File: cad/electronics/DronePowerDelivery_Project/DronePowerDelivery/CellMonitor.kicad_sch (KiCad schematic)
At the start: 12 parts, among them J1 Conn_01x05_Socket, J2 Conn_01x02_Socket, U1 BQ76920PW

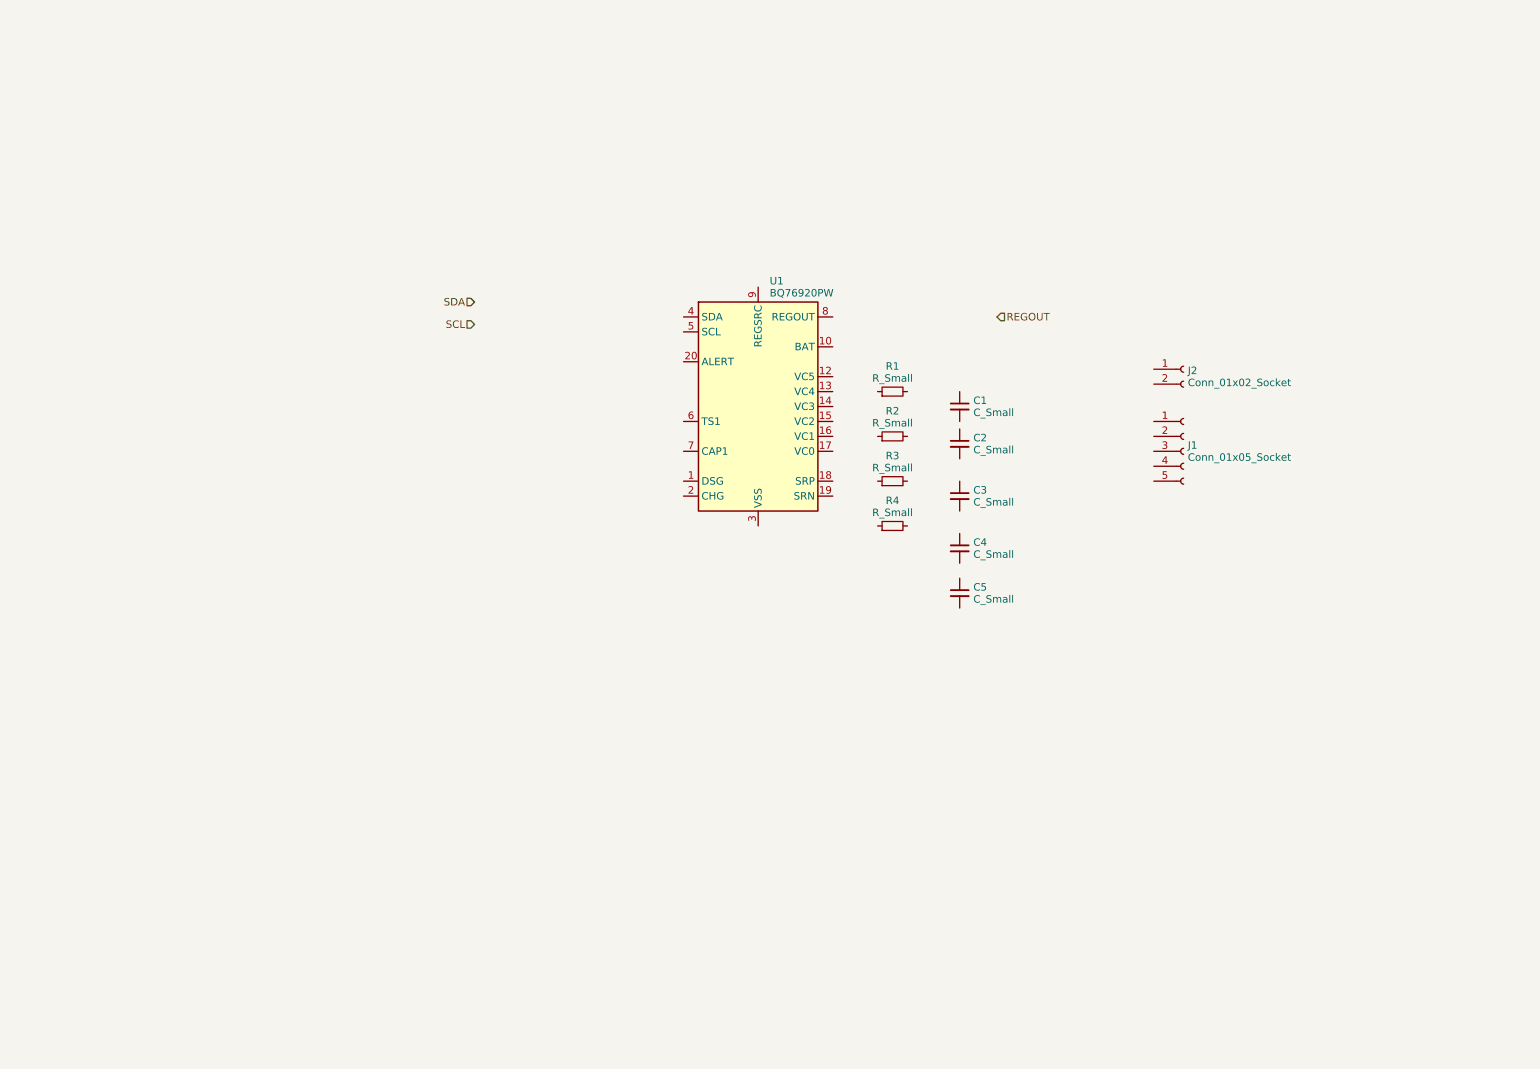
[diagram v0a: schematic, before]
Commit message: Added additional schematic capture
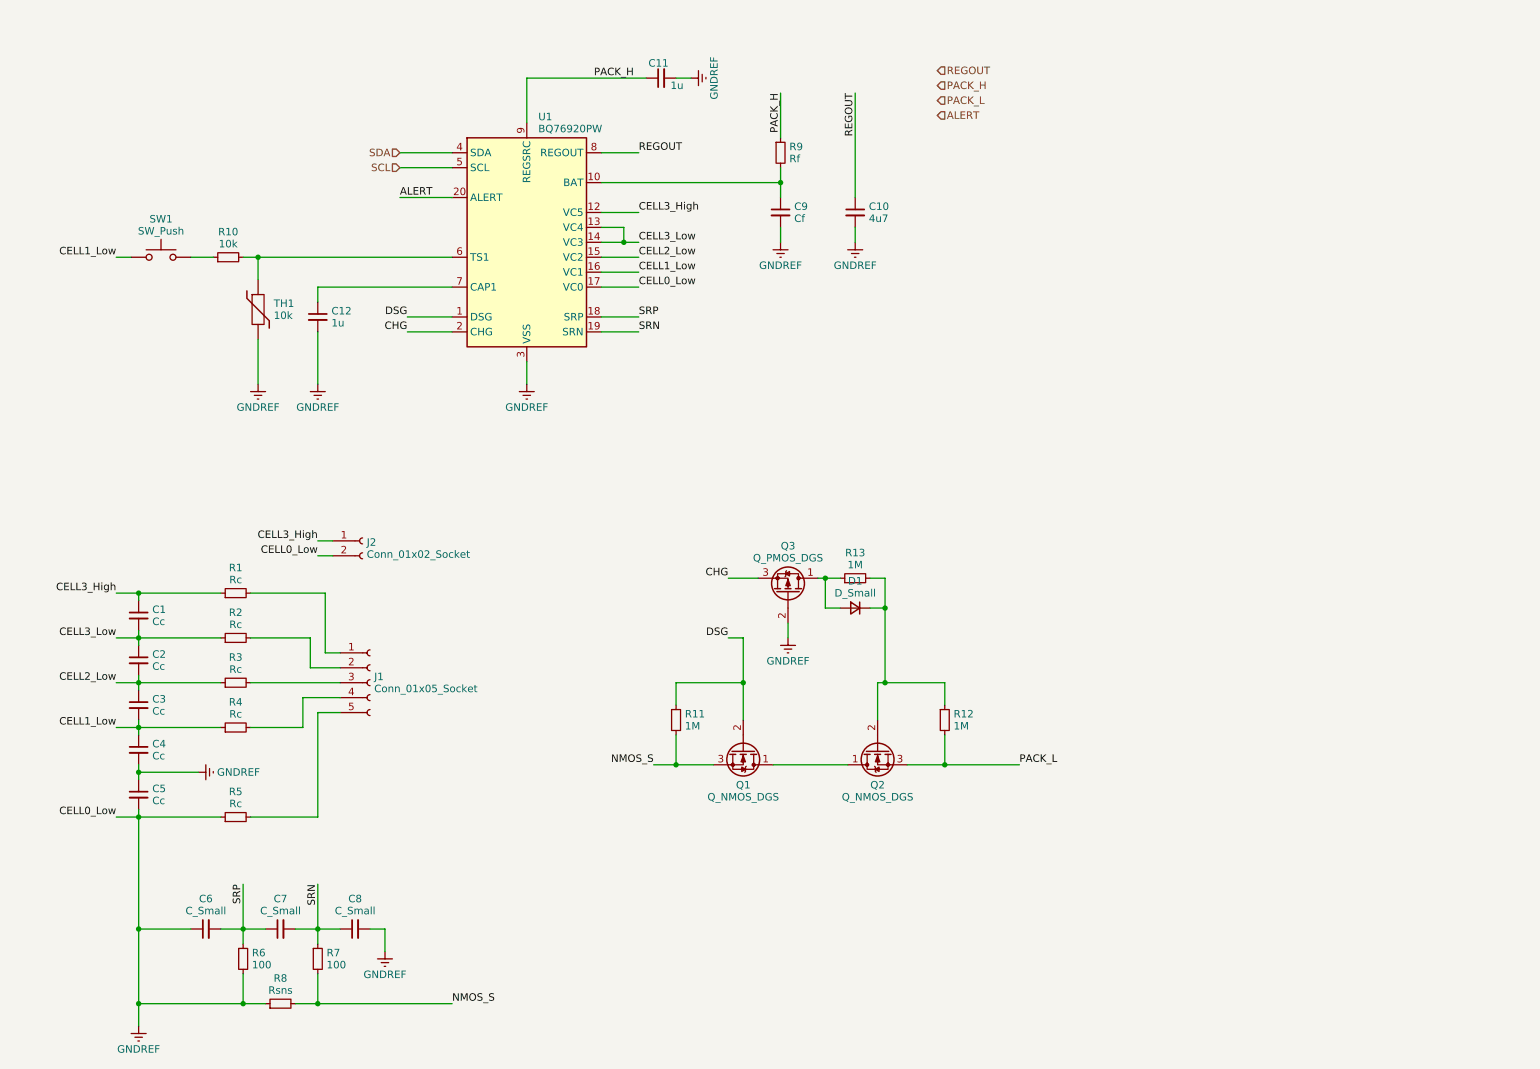
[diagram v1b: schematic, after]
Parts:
- added C10: 4u7, symbol Device:C_Small
- added C11, C12: 1u, symbol Device:C_Small
- added C6, C7, C8: C_Small, symbol Device:C_Small
- added C9: Cf, symbol Device:C_Small
- added D1: D_Small, symbol Device:D_Small
- added Q1, Q2: Q_NMOS_DGS, symbol Device:Q_NMOS_DGS
- added Q3: Q_PMOS_DGS, symbol Device:Q_PMOS_DGS
- added R10: 10k, symbol Device:R_Small
- added R11, R12, R13: 1M, symbol Device:R_Small
- added R5: Rc, symbol Device:R_Small
- added R6, R7: 100, symbol Device:R_Small
- added R8: Rsns, symbol Device:R_Small
- added R9: Rf, symbol Device:R_Small
- added SW1: SW_Push, symbol Switch:SW_Push
- added TH1: 10k, symbol Device:Thermistor
- C1, C2, C3, C4, C5: value C_Small -> Cc
- R1, R2, R3, R4: value R_Small -> Rc
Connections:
- net REGOUT: now also U1.8 (REGOUT), C10.1
- net SCL: now also U1.5 (SCL)
- net SDA: now also U1.4 (SDA)
- net CELL3_High: now reaches C1.1
- net CELL3_High: now also J2.1 (Pin_1), R1.1, U1.12 (VC5)
- net CELL3_Low: now reaches C1.2
- net CELL3_Low: now also C2.1, R2.1, U1.13 (VC4), U1.14 (VC3)
- net at J1.1 (Pin_1): now also R1.2
- net at J1.2 (Pin_2): now also R2.2
- net at J1.3 (Pin_3): now also R3.2
- net at J1.4 (Pin_4): now also R4.2
- net at J1.5 (Pin_5): now also R5.2
- net CELL2_Low: now reaches C3.1
- net CELL2_Low: now also C2.2, R3.1, U1.15 (VC2)
- net CELL1_Low: now reaches C3.2
- net CELL1_Low: now also C4.1, R4.1, U1.16 (VC1), SW1.1
- net GNDREF: now reaches C4.2
- net GNDREF: now also C5.1, C5.2, J2.2 (Pin_2), U1.17 (VC0), U1.3 (VSS), C10.2, C11.2, C12.2, C6.1, C8.2, C9.2, Q3.2 (G), R5.1, R6.2, R8.1, TH1.2
- net DSG: now reaches U1.1 (DSG)
- net DSG: now also Q1.2 (G), R11.1
- net at U1.10 (BAT): now also C9.1, R9.2
- net SRP: now reaches U1.18 (SRP)
- net SRP: now also C6.2, C7.1, R6.1
- net SRN: now reaches U1.19 (SRN)
- net SRN: now also C7.2, C8.1, R7.1
- net CHG: now reaches U1.2 (CHG)
- net CHG: now also Q3.3 (S)
- net ALERT: now reaches U1.20 (ALERT)
- net at U1.6 (TS1): now also R10.2, TH1.1
- net at U1.7 (CAP1): now also C12.1
- net PACK_H: now reaches U1.9 (REGSRC)
- net PACK_H: now also C11.1, R9.1
- new net: R10.1, SW1.2
- new net: Q1.1 (D), Q2.1 (D)
- new net: D1.1 (K), Q2.2 (G), R12.1, R13.2
- new net: D1.2 (A), Q3.1 (D), R13.1
- new net NMOS_S: Q1.3 (S), R11.2, R7.2, R8.2
- new net PACK_L: Q2.3 (S), R12.2
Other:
- moved on the sheet: C1, C2, C3, C4, C5, J1, J2, R1, R2, R3, R4, U1

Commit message: Finialized Component Sizing
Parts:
- removed Q1, Q2: Q_NMOS_DGS, symbol Device:Q_NMOS_DGS
- removed Q3: Q_PMOS_DGS, symbol Device:Q_PMOS_DGS
- added Q1, Q2: Q_NMOS_GDS, Package_TO_SOT_SMD:TO-252-2, symbol Device:Q_NMOS_GDS
- added Q3: Q_PMOS_GSD, Package_TO_SOT_SMD:SOT-23, symbol Device:Q_PMOS_GSD
- C1, C10, C11, C12, C2, C3, C4, C5, C6, C7, C8, C9: footprint (none) -> Capacitor_SMD:C_0603_1608Metric
- D1: footprint (none) -> Diode_SMD:D_0603_1608Metric
- J1: footprint (none) -> Connector_JST:JST_XH_B5B-XH-A_1x05_P2.50mm_Vertical
- J2: footprint (none) -> Connector_AMASS:AMASS_XT60-F_1x02_P7.20mm_Vertical
- R1, R10, R11, R12, R13, R2, R3, R4, R5, R6, R7, R9, TH1: footprint (none) -> Resistor_SMD:R_0603_1608Metric
- R8: footprint (none) -> Resistor_SMD:R_2512_6332Metric
- SW1: footprint (none) -> Button_Switch_SMD:SW_SPST_EVQP2; Mfg Part# (none) -> EVQ-P2002W
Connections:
- net CELL3_High: no longer J2.1 (Pin_1)
- net CHG: now also Q3.2 (S)
- net DSG: now also Q1.1 (G)
- net GNDREF: now also J1.5 (Pin_5), J2.1 (Pin_1), R5.2, Q3.1 (G); no longer C5.2, J2.2 (Pin_2), R5.1, U1.17 (VC0)
- net PACK_H: now also J1.1 (Pin_1), J2.2 (Pin_2), R1.2
- net PACK_L: now also Q2.3 (S)
- net IN_PROT: now reaches D1.1 (K), R12.1, R13.2
- net IN_PROT: now also Q2.1 (G)
- net at D1.2 (A), R13.1: now also Q3.3 (D)
- net NMOS_S renamed Q1_SRC
- net Q1_SRC: now also Q1.3 (S)
- new net CELL0_Low: C5.2, R5.1, U1.17 (VC0)
- new net Q_DRN: Q1.2 (D), Q2.2 (D)
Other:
- note added: "Cell Voltage Probes & Balacing"
- note added: "Charge/Discharge Control Circuit"
- note added: "Current Sense Circuit"
- moved on the sheet: D1, J2, R11, R12, R13

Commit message: Assigned component values
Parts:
- C1, C2, C3, C4, C5: value Cc -> 1uf
- C6, C7, C8: value C_Small -> 0.1uf
- C9: value Cf -> 10uf
- R1, R2, R3, R4, R5: value Rc -> 100
- R9: value Rf -> 100
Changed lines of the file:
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@@
   (symbol (lib_id "Device:R_Small") (at 154.94 38.1 0) (unit 1)
     (in_bom yes) (on_board yes) (dnp no) (fields_autoplaced)
-    (property "Reference" "R9" (at 156.4386 37.076 0)
-      (effects (font (size 1.27 1.27)) (justify left))
-    )
-    (property "Value" "Rf" (at 156.4386 39.124 0)
+    (property "Reference" "R9" (at 156.4386 36.8879 0)
+      (effects (font (size 1.27 1.27)) (justify left))
+    )
+    (property "Value" "100" (at 156.4386 39.3121 0)
       (effects (font (size 1.27 1.27)) (justify left))
     )
@@
   (symbol (lib_id "Device:C_Small") (at 45.72 116.84 0) (unit 1)
     (in_bom yes) (on_board yes) (dnp no) (fields_autoplaced)
-    (property "Reference" "C1" (at 48.0441 115.8223 0)
-      (effects (font (size 1.27 1.27)) (justify left))
-    )
-    (property "Value" "Cc" (at 48.0441 117.8703 0)
+    (property "Reference" "C1" (at 48.0441 115.6342 0)
+      (effects (font (size 1.27 1.27)) (justify left))
+    )
+    (property "Value" "1uf" (at 48.0441 118.0584 0)
       (effects (font (size 1.27 1.27)) (justify left))
     )
@@
   (symbol (lib_id "Device:C_Small") (at 57.15 170.18 90) (unit 1)
     (in_bom yes) (on_board yes) (dnp no) (fields_autoplaced)
-    (property "Reference" "C6" (at 57.1563 165.0379 90)
-      (effects (font (size 1.27 1.27)))
-    )
-    (property "Value" "C_Small" (at 57.1563 167.0859 90)
+    (property "Reference" "C6" (at 57.1563 164.4736 90)
+      (effects (font (size 1.27 1.27)))
+    )
+    (property "Value" "0.1uf" (at 57.1563 166.8978 90)
       (effects (font (size 1.27 1.27)))
     )
@@
   (symbol (lib_id "Device:R_Small") (at 62.23 151.13 90) (unit 1)
     (in_bom yes) (on_board yes) (dnp no) (fields_autoplaced)
-    (property "Reference" "R5" (at 62.23 146.8134 90)
-      (effects (font (size 1.27 1.27)))
-    )
-    (property "Value" "Rc" (at 62.23 148.8614 90)
+    (property "Reference" "R5" (at 62.23 146.2491 90)
+      (effects (font (size 1.27 1.27)))
+    )
+    (property "Value" "100" (at 62.23 148.6733 90)
       (effects (font (size 1.27 1.27)))
     )
@@
   (symbol (lib_id "Device:C_Small") (at 69.85 170.18 90) (unit 1)
     (in_bom yes) (on_board yes) (dnp no) (fields_autoplaced)
-    (property "Reference" "C7" (at 69.8563 165.0379 90)
-      (effects (font (size 1.27 1.27)))
-    )
-    (property "Value" "C_Small" (at 69.8563 167.0859 90)
+    (property "Reference" "C7" (at 69.8563 164.4736 90)
+      (effects (font (size 1.27 1.27)))
+    )
+    (property "Value" "0.1uf" (at 69.8563 166.8978 90)
       (effects (font (size 1.27 1.27)))
     )
@@
   (symbol (lib_id "Device:C_Small") (at 45.72 132.08 0) (unit 1)
     (in_bom yes) (on_board yes) (dnp no) (fields_autoplaced)
-    (property "Reference" "C3" (at 48.0441 131.0623 0)
-      (effects (font (size 1.27 1.27)) (justify left))
-    )
-    (property "Value" "Cc" (at 48.0441 133.1103 0)
+    (property "Reference" "C3" (at 48.0441 130.8742 0)
+      (effects (font (size 1.27 1.27)) (justify left))
+    )
+    (property "Value" "1uf" (at 48.0441 133.2984 0)
       (effects (font (size 1.27 1.27)) (justify left))
     )
@@
   (symbol (lib_id "Device:C_Small") (at 82.55 170.18 90) (unit 1)
     (in_bom yes) (on_board yes) (dnp no) (fields_autoplaced)
-    (property "Reference" "C8" (at 82.5563 165.0379 90)
-      (effects (font (size 1.27 1.27)))
-    )
-    (property "Value" "C_Small" (at 82.5563 167.0859 90)
+    (property "Reference" "C8" (at 82.5563 164.4736 90)
+      (effects (font (size 1.27 1.27)))
+    )
+    (property "Value" "0.1uf" (at 82.5563 166.8978 90)
       (effects (font (size 1.27 1.27)))
     )
@@
   (symbol (lib_id "Device:C_Small") (at 45.72 139.7 0) (unit 1)
     (in_bom yes) (on_board yes) (dnp no) (fields_autoplaced)
-    (property "Reference" "C4" (at 48.0441 138.6823 0)
-      (effects (font (size 1.27 1.27)) (justify left))
-    )
-    (property "Value" "Cc" (at 48.0441 140.7303 0)
+    (property "Reference" "C4" (at 48.0441 138.4942 0)
+      (effects (font (size 1.27 1.27)) (justify left))
+    )
+    (property "Value" "1uf" (at 48.0441 140.9184 0)
       (effects (font (size 1.27 1.27)) (justify left))
     )
@@
   (symbol (lib_id "Device:C_Small") (at 154.94 48.26 0) (unit 1)
     (in_bom yes) (on_board yes) (dnp no) (fields_autoplaced)
-    (property "Reference" "C9" (at 157.2641 47.2423 0)
-      (effects (font (size 1.27 1.27)) (justify left))
-    )
-    (property "Value" "Cf" (at 157.2641 49.2903 0)
+    (property "Reference" "C9" (at 157.2641 47.0542 0)
+      (effects (font (size 1.27 1.27)) (justify left))
+    )
+    (property "Value" "10uf" (at 157.2641 49.4784 0)
       (effects (font (size 1.27 1.27)) (justify left))
     )
@@
   (symbol (lib_id "Device:R_Small") (at 62.23 128.27 90) (unit 1)
     (in_bom yes) (on_board yes) (dnp no) (fields_autoplaced)
-    (property "Reference" "R3" (at 62.23 123.9534 90)
-      (effects (font (size 1.27 1.27)))
-    )
-    (property "Value" "Rc" (at 62.23 126.0014 90)
+    (property "Reference" "R3" (at 62.23 123.3891 90)
+      (effects (font (size 1.27 1.27)))
+    )
+    (property "Value" "100" (at 62.23 125.8133 90)
       (effects (font (size 1.27 1.27)))
     )
@@
   (symbol (lib_id "Device:C_Small") (at 45.72 124.46 0) (unit 1)
     (in_bom yes) (on_board yes) (dnp no) (fields_autoplaced)
-    (property "Reference" "C2" (at 48.0441 123.4423 0)
-      (effects (font (size 1.27 1.27)) (justify left))
-    )
-    (property "Value" "Cc" (at 48.0441 125.4903 0)
+    (property "Reference" "C2" (at 48.0441 123.2542 0)
+      (effects (font (size 1.27 1.27)) (justify left))
+    )
+    (property "Value" "1uf" (at 48.0441 125.6784 0)
       (effects (font (size 1.27 1.27)) (justify left))
     )
@@
   (symbol (lib_id "Device:R_Small") (at 62.23 120.65 90) (unit 1)
     (in_bom yes) (on_board yes) (dnp no) (fields_autoplaced)
-    (property "Reference" "R2" (at 62.23 116.3334 90)
-      (effects (font (size 1.27 1.27)))
-    )
-    (property "Value" "Rc" (at 62.23 118.3814 90)
+    (property "Reference" "R2" (at 62.23 115.7691 90)
+      (effects (font (size 1.27 1.27)))
+    )
+    (property "Value" "100" (at 62.23 118.1933 90)
       (effects (font (size 1.27 1.27)))
     )
@@
   (symbol (lib_id "Device:R_Small") (at 62.23 135.89 90) (unit 1)
     (in_bom yes) (on_board yes) (dnp no) (fields_autoplaced)
-    (property "Reference" "R4" (at 62.23 131.5734 90)
-      (effects (font (size 1.27 1.27)))
-    )
-    (property "Value" "Rc" (at 62.23 133.6214 90)
+    (property "Reference" "R4" (at 62.23 131.0091 90)
+      (effects (font (size 1.27 1.27)))
+    )
+    (property "Value" "100" (at 62.23 133.4333 90)
       (effects (font (size 1.27 1.27)))
     )
@@
   (symbol (lib_id "Device:C_Small") (at 45.72 147.32 0) (unit 1)
     (in_bom yes) (on_board yes) (dnp no) (fields_autoplaced)
-    (property "Reference" "C5" (at 48.0441 146.3023 0)
-      (effects (font (size 1.27 1.27)) (justify left))
-    )
-    (property "Value" "Cc" (at 48.0441 148.3503 0)
+    (property "Reference" "C5" (at 48.0441 146.1142 0)
+      (effects (font (size 1.27 1.27)) (justify left))
+    )
+    (property "Value" "1uf" (at 48.0441 148.5384 0)
       (effects (font (size 1.27 1.27)) (justify left))
     )
@@
   (symbol (lib_id "Device:R_Small") (at 62.23 113.03 90) (unit 1)
     (in_bom yes) (on_board yes) (dnp no) (fields_autoplaced)
-    (property "Reference" "R1" (at 62.23 108.7134 90)
-      (effects (font (size 1.27 1.27)))
-    )
-    (property "Value" "Rc" (at 62.23 110.7614 90)
-      (effects (font (size 1.27 1.27)))
-    )
+    (property "Reference" "R1" (at 62.23 108.1491 90)
+      (effects (font (size 1.27 1.27)))
+    )
+    (property "Value" "100" (at 62.23 110.5733 90)
+      (effects (font (size 1.27 1.27)))
+    )
